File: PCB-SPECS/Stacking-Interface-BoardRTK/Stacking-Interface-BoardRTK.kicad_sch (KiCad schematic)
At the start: 0 parts

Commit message: Update
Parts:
- added ESP_Left, ESP_Right: Conn_01x15_Socket, symbol Connector:Conn_01x15_Socket
- added RTK_Bottom_Left: Conn_01x10_Pin, symbol Connector:Conn_01x10_Pin
- added RTK_Bottom_Right, RTK_Top_Left: Conn_01x08_Pin, symbol Connector:Conn_01x08_Pin
- added RTK_Top_Right: Conn_01x06_Pin, symbol Connector:Conn_01x06_Pin

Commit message: updates
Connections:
- net GND: now also ESP_Right.14 (Pin_14), RTK_Bottom_Right.1 (Pin_1), RTK_Bottom_Right.2 (Pin_2)
- net at ESP_Right.10 (Pin_10): now also RTK_Top_Left.1 (TX1)

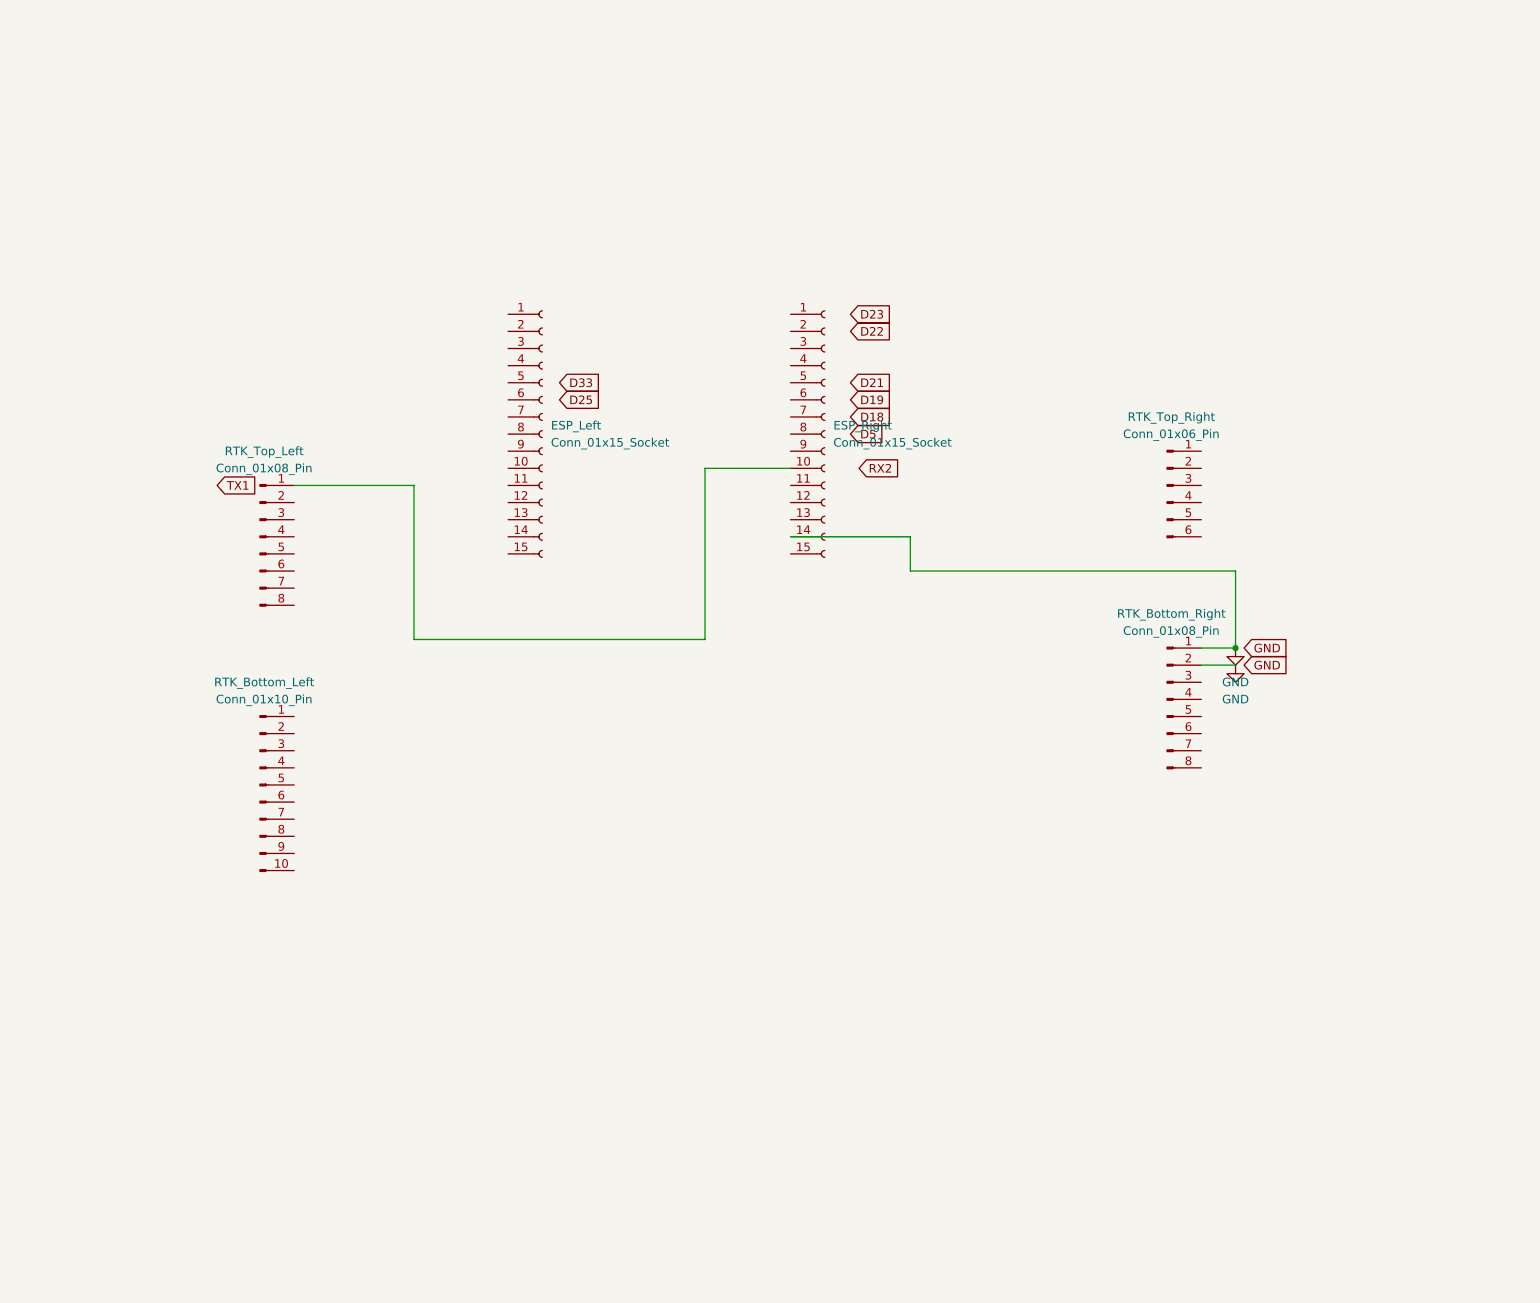
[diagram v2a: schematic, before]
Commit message: Updates to schematic, now all include digital footprints
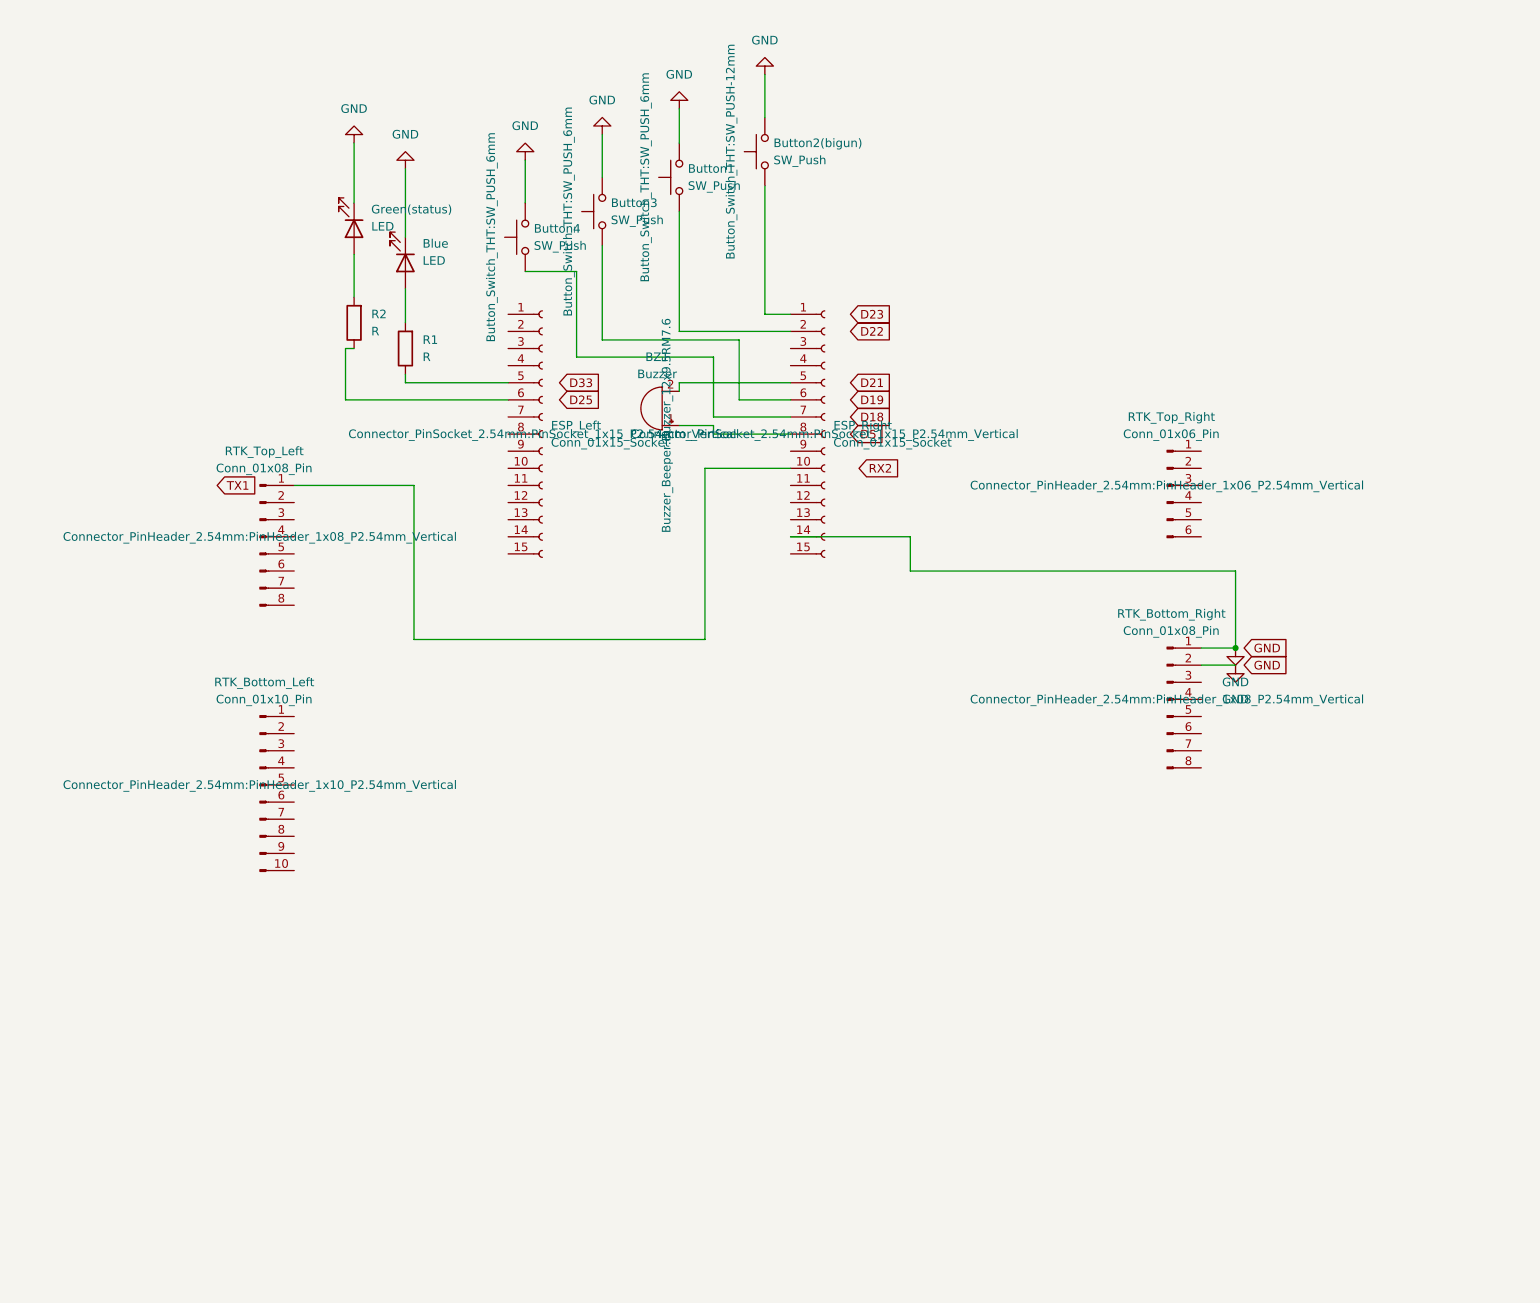
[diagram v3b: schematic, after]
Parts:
- added BZ1: Buzzer, Buzzer_Beeper:Buzzer_12x9.5RM7.6, symbol Device:Buzzer
- added Blue, Green(status): LED, LED_SMD:LED_0603_1608Metric, symbol Device:LED
- added Button1, Button3, Button4: SW_Push, Button_Switch_THT:SW_PUSH_6mm, symbol Switch:SW_Push
- added Button2(bigun): SW_Push, Button_Switch_THT:SW_PUSH-12mm, symbol Switch:SW_Push
- added R1, R2: R, Resistor_THT:R_Axial_DIN0207_L6.3mm_D2.5mm_P10.16mm_Horizontal, symbol Device:R
- ESP_Left, ESP_Right: footprint (none) -> Connector_PinSocket_2.54mm:PinSocket_1x15_P2.54mm_Vertical
- RTK_Bottom_Left: footprint (none) -> Connector_PinHeader_2.54mm:PinHeader_1x10_P2.54mm_Vertical
- RTK_Bottom_Right, RTK_Top_Left: footprint (none) -> Connector_PinHeader_2.54mm:PinHeader_1x08_P2.54mm_Vertical
- RTK_Top_Right: footprint (none) -> Connector_PinHeader_2.54mm:PinHeader_1x06_P2.54mm_Vertical
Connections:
- net GND: now also Blue.1 (K), Button1.2, Button2(bigun).2, Button3.2, Button4.2, Green(status).1 (K)
- net at ESP_Right.1 (Pin_1): now also Button2(bigun).1
- net at ESP_Right.2 (Pin_2): now also Button1.1
- net at ESP_Right.5 (Pin_5): now also BZ1.2 (-)
- net at ESP_Right.6 (Pin_6): now also Button3.1
- net at ESP_Right.7 (Pin_7): now also Button4.1
- net at ESP_Right.8 (Pin_8): now also BZ1.1 (+)
- net at ESP_Left.5 (Pin_5): now also R1.1
- net at ESP_Left.6 (Pin_6): now also R2.1
- new net: Blue.2 (A), R1.2
- new net: Green(status).2 (A), R2.2

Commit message: Okay Have a PCB design still need to measure the actual pins to make sure it's 100% accurate and figure out the fill and such
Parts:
- D1: renamed from Blue; value LED -> Blue
- D2: renamed from Green(status); value LED -> Green(Status)
- renumbered Button2(bigun) to Button2(bigun)1, ESP_Left to ESP_Left1, ESP_Right to ESP_Right1, RTK_Bottom_Left to RTK_Bottom_Left1, RTK_Bottom_Right to RTK_Bottom_Right1, RTK_Top_Left to RTK_Top_Left1, RTK_Top_Right to RTK_Top_Right1
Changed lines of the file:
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@@
 		(color 0 0 0 0)
 	)
+	(junction
+		(at 215.9 99.06)
+		(diameter 0)
+		(color 0 0 0 0)
+	)
 	(wire
 		(pts
@@
 	(wire
 		(pts
-			(xy 215.9 106.68) (xy 215.9 95.25)
+			(xy 215.9 106.68) (xy 215.9 99.06)
 		)
 		(stroke
@@
 	(wire
 		(pts
+			(xy 215.9 99.06) (xy 227.33 99.06)
+		)
+		(stroke
+			(width 0)
+			(type default)
+		)
+	)
+	(wire
+		(pts
 			(xy 149.86 69.85) (xy 142.24 69.85)
+		)
+		(stroke
+			(width 0)
+			(type default)
+		)
+	)
+	(wire
+		(pts
+			(xy 215.9 99.06) (xy 215.9 95.25)
 		)
 		(stroke
@@
 		(dnp no)
 		(fields_autoplaced yes)
-		(property "Reference" "RTK_Top_Right"
+		(property "Reference" "RTK_Top_Right1"
 			(at 206.375 72.39 0)
 			(effects
@@
 			(project ""
 				(path "/1750928f-7fe5-4459-8ec0-df0c49a4147a"
-					(reference "RTK_Top_Right")
+					(reference "RTK_Top_Right1")
 					(unit 1)
 				)
@@
 		(dnp no)
 		(fields_autoplaced yes)
-		(property "Reference" "Blue"
+		(property "Reference" "D1"
 			(at 95.25 46.6724 90)
 			(effects
@@
 			)
 		)
-		(property "Value" "LED"
+		(property "Value" "Blue"
 			(at 95.25 49.2124 90)
 			(effects
@@
 			(project ""
 				(path "/1750928f-7fe5-4459-8ec0-df0c49a4147a"
-					(reference "Blue")
+					(reference "D1")
 					(unit 1)
 				)
@@
 		(dnp no)
 		(fields_autoplaced yes)
-		(property "Reference" "Green(status)"
+		(property "Reference" "D2"
 			(at 87.63 41.5924 90)
 			(effects
@@
 			)
 		)
-		(property "Value" "LED"
+		(property "Value" "Green(Status)"
 			(at 87.63 44.1324 90)
 			(effects
@@
 			(project ""
 				(path "/1750928f-7fe5-4459-8ec0-df0c49a4147a"
-					(reference "Green(status)")
+					(reference "D2")
 					(unit 1)
 				)
@@
 		(dnp no)
 		(fields_autoplaced yes)
-		(property "Reference" "ESP_Right"
+		(property "Reference" "ESP_Right1"
 			(at 156.21 73.6599 0)
 			(effects
@@
 			(project ""
 				(path "/1750928f-7fe5-4459-8ec0-df0c49a4147a"
-					(reference "ESP_Right")
+					(reference "ESP_Right1")
 					(unit 1)
 				)
@@
 		(dnp no)
 		(fields_autoplaced yes)
-		(property "Reference" "RTK_Bottom_Left"
+		(property "Reference" "RTK_Bottom_Left1"
 			(at 71.755 111.76 0)
 			(effects
@@
 			(project ""
 				(path "/1750928f-7fe5-4459-8ec0-df0c49a4147a"
-					(reference "RTK_Bottom_Left")
+					(reference "RTK_Bottom_Left1")
 					(unit 1)
 				)
@@
 		(dnp no)
 		(fields_autoplaced yes)
-		(property "Reference" "ESP_Left"
+		(property "Reference" "ESP_Left1"
 			(at 114.3 73.6599 0)
 			(effects
@@
 			(project ""
 				(path "/1750928f-7fe5-4459-8ec0-df0c49a4147a"
-					(reference "ESP_Left")
+					(reference "ESP_Left1")
 					(unit 1)
 				)
@@
 		(dnp no)
 		(fields_autoplaced yes)
-		(property "Reference" "Button2(bigun)"
+		(property "Reference" "Button2(bigun)1"
 			(at 147.32 31.7499 90)
 			(effects
@@
 			(project ""
 				(path "/1750928f-7fe5-4459-8ec0-df0c49a4147a"
-					(reference "Button2(bigun)")
+					(reference "Button2(bigun)1")
 					(unit 1)
 				)
@@
 		(dnp no)
 		(fields_autoplaced yes)
-		(property "Reference" "RTK_Top_Left"
+		(property "Reference" "RTK_Top_Left1"
 			(at 71.755 77.47 0)
 			(effects
@@
 			(project ""
 				(path "/1750928f-7fe5-4459-8ec0-df0c49a4147a"
-					(reference "RTK_Top_Left")
+					(reference "RTK_Top_Left1")
 					(unit 1)
 				)
@@
 	)
 	(symbol
+		(lib_id "power:PWR_FLAG")
+		(at 227.33 99.06 0)
+		(unit 1)
+		(exclude_from_sim no)
+		(in_bom yes)
+		(on_board yes)
+		(dnp no)
+		(fields_autoplaced yes)
+		(property "Reference" "#FLG01"
+			(at 227.33 97.155 0)
+			(effects
+				(font
+					(size 1.27 1.27)
+				)
+				(hide yes)
+			)
+		)
+		(property "Value" "PWR_FLAG"
+			(at 227.33 93.98 0)
+			(effects
+				(font
+					(size 1.27 1.27)
+				)
+			)
+		)
+		(property "Footprint" ""
+			(at 227.33 99.06 0)
+			(effects
+				(font
+					(size 1.27 1.27)
+				)
+				(hide yes)
+			)
+		)
+		(property "Datasheet" "~"
+			(at 227.33 99.06 0)
+			(effects
+				(font
+					(size 1.27 1.27)
+				)
+				(hide yes)
+			)
+		)
+		(property "Description" "Special symbol for telling ERC where power comes from"
+			(at 227.33 99.06 0)
+			(effects
+				(font
+					(size 1.27 1.27)
+				)
+				(hide yes)
+			)
+		)
+		(pin "1"
+		)
+		(instances
+			(project ""
+				(path "/1750928f-7fe5-4459-8ec0-df0c49a4147a"
+					(reference "#FLG01")
+					(unit 1)
+				)
+			)
+		)
+	)
+	(symbol
 		(lib_id "power:GND")
 		(at 92.71 35.56 180)
@@
 		(dnp no)
 		(fields_autoplaced yes)
-		(property "Reference" "RTK_Bottom_Right"
+		(property "Reference" "RTK_Bottom_Right1"
 			(at 206.375 101.6 0)
 			(effects
@@
 			(project ""
 				(path "/1750928f-7fe5-4459-8ec0-df0c49a4147a"
-					(reference "RTK_Bottom_Right")
+					(reference "RTK_Bottom_Right1")
 					(unit 1)
 				)
